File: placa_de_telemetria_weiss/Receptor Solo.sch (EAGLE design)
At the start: 6 parts

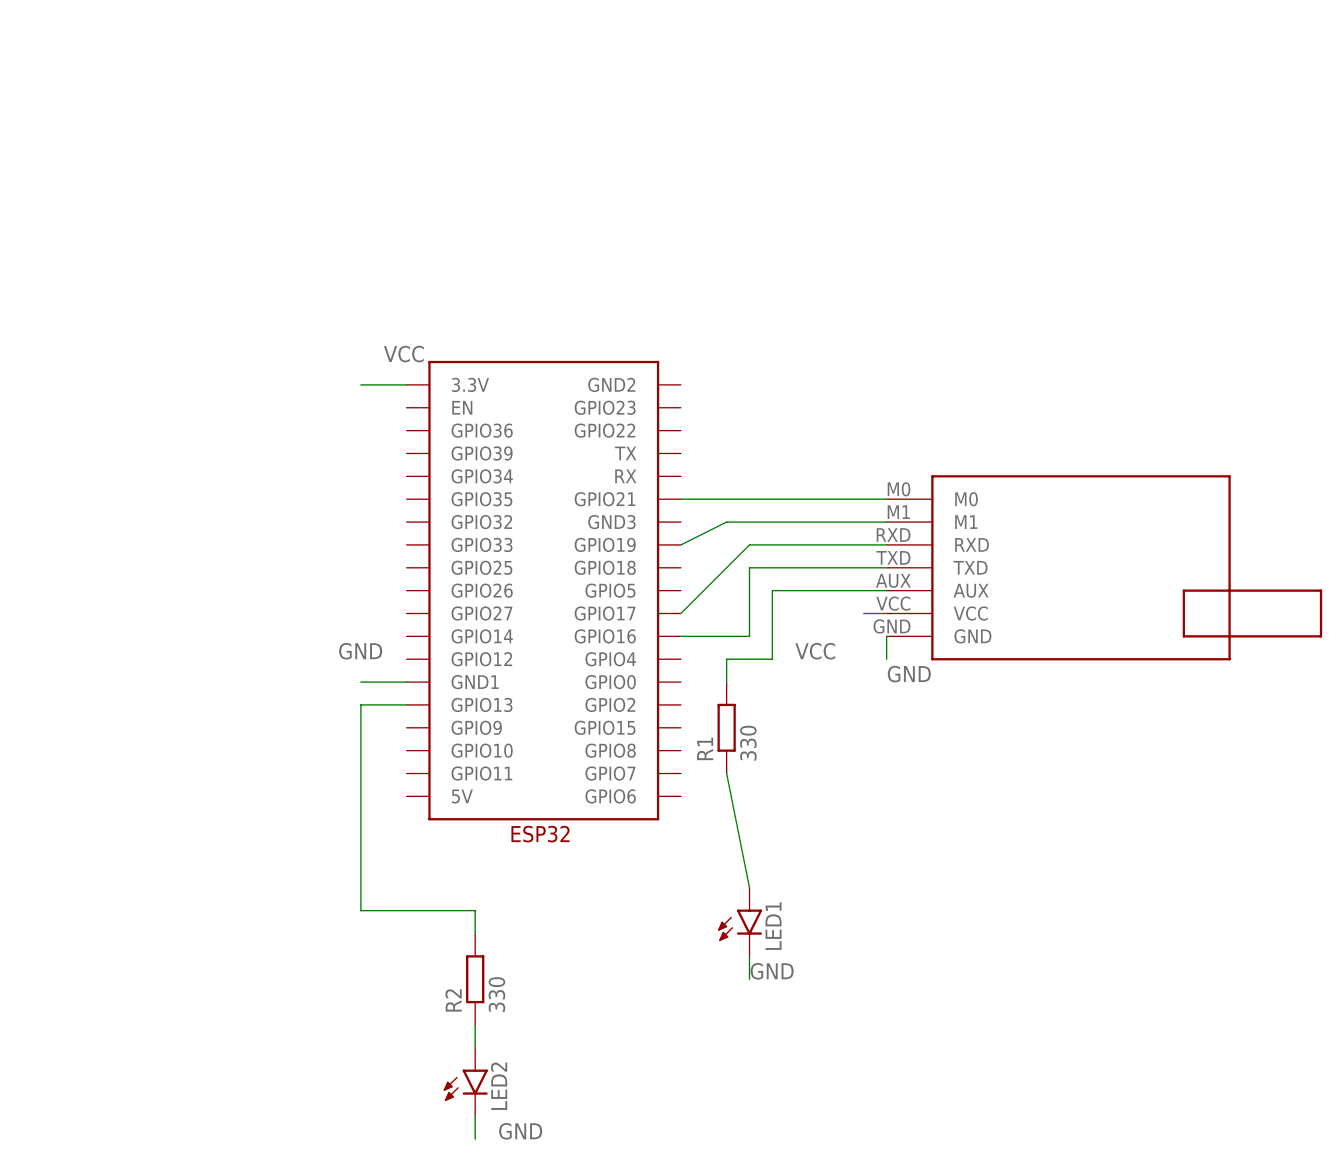
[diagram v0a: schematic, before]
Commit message: fix(pcb): substitui ESP32 incorreto e adiciona furos de fixação à placa de telemetria
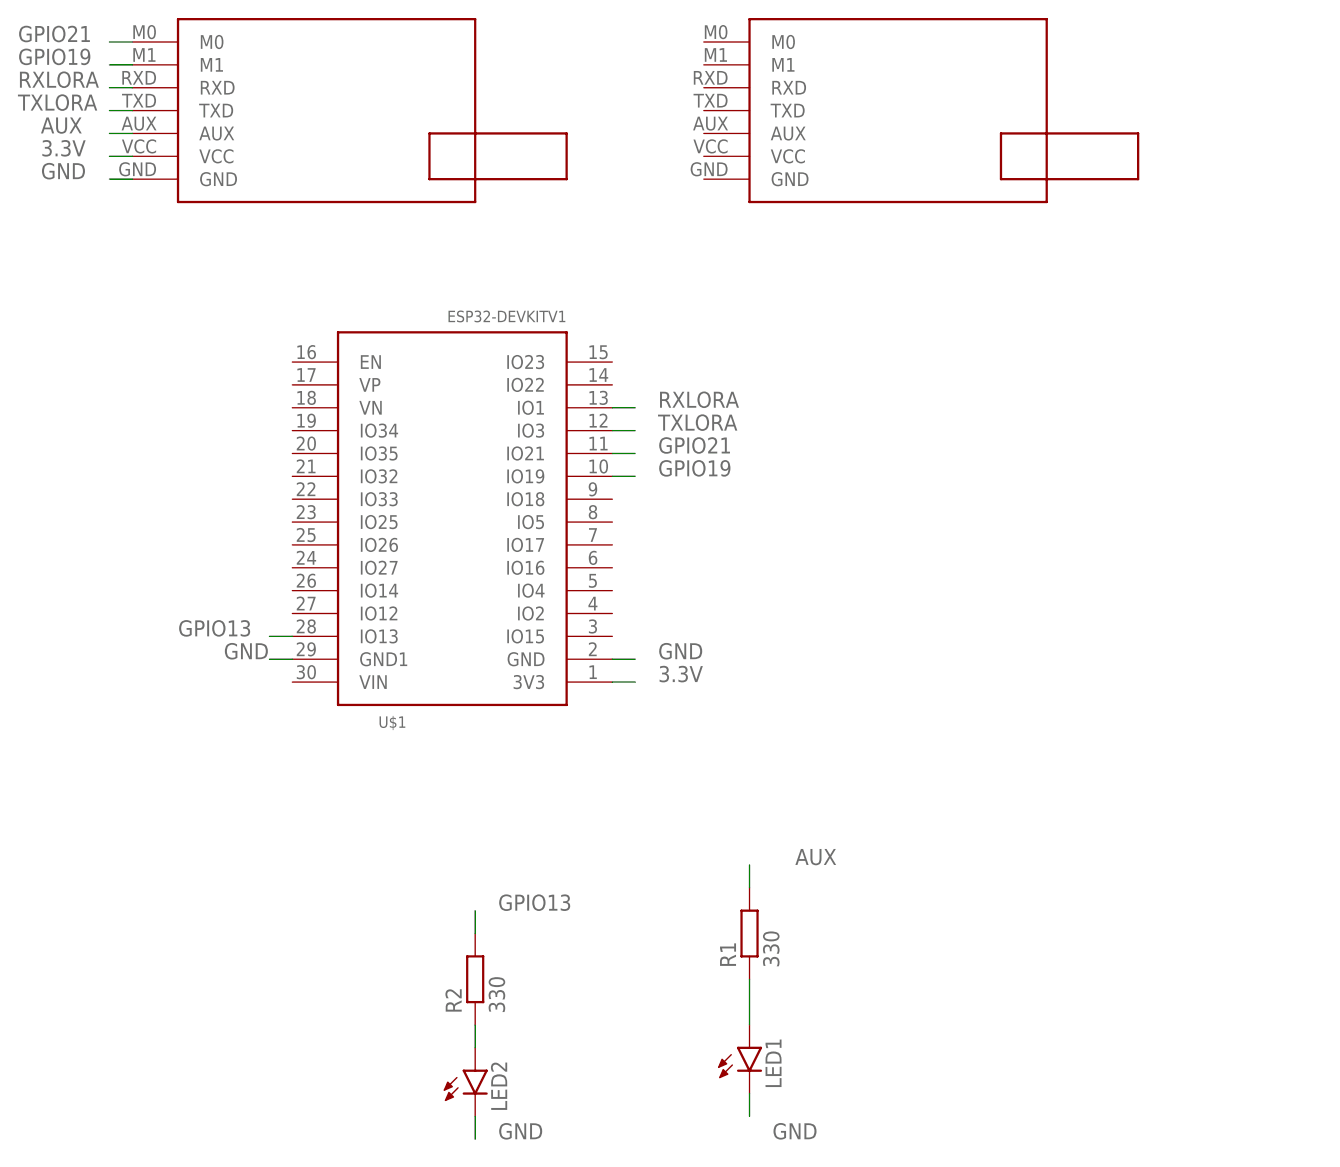
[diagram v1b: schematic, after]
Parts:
- added FUROSDEAPOIOLORA: E22-400T30D, CRD:E22-400T30D
- U$1: value ESP32 -> ESP32DEVKITV1; device esp32:ESP32 -> ESP32-DEVKITV1:ESP32DEVKITV1
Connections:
- net N$6 renamed AUX
- removed net N$1: U$1.GPIO21, U$2.M0
- removed net N$2: U$1.GPIO19, U$2.M1
- removed net N$3: U$1.GPIO17, U$2.RXD
- removed net N$4: U$1.GPIO16, U$2.TXD
- removed net N$5: R2.2, U$1.GPIO13
- removed net VCC: U$1.3.3V, U$2.VCC
- new net 3.3V: U$1.3V3, U$2.VCC
- new net GPIO13: R2.2, U$1.IO13
- new net GPIO19: U$1.IO19, U$2.M1
- new net GPIO21: U$1.IO21, U$2.M0
- new net RXLORA: U$1.IO1, U$2.RXD
- new net TXLORA: U$1.IO3, U$2.TXD
- net GND: now also U$1.GND
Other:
- moved on the sheet: LED1, R1
